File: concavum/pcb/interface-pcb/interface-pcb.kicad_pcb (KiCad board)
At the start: 2 copper layers, 36 x 42 mm, 11 parts, among them J1 Audio_Jack, J2 FPC_connector, U1 Adafruit_KB2040, U2 MCP23017/MCP23018

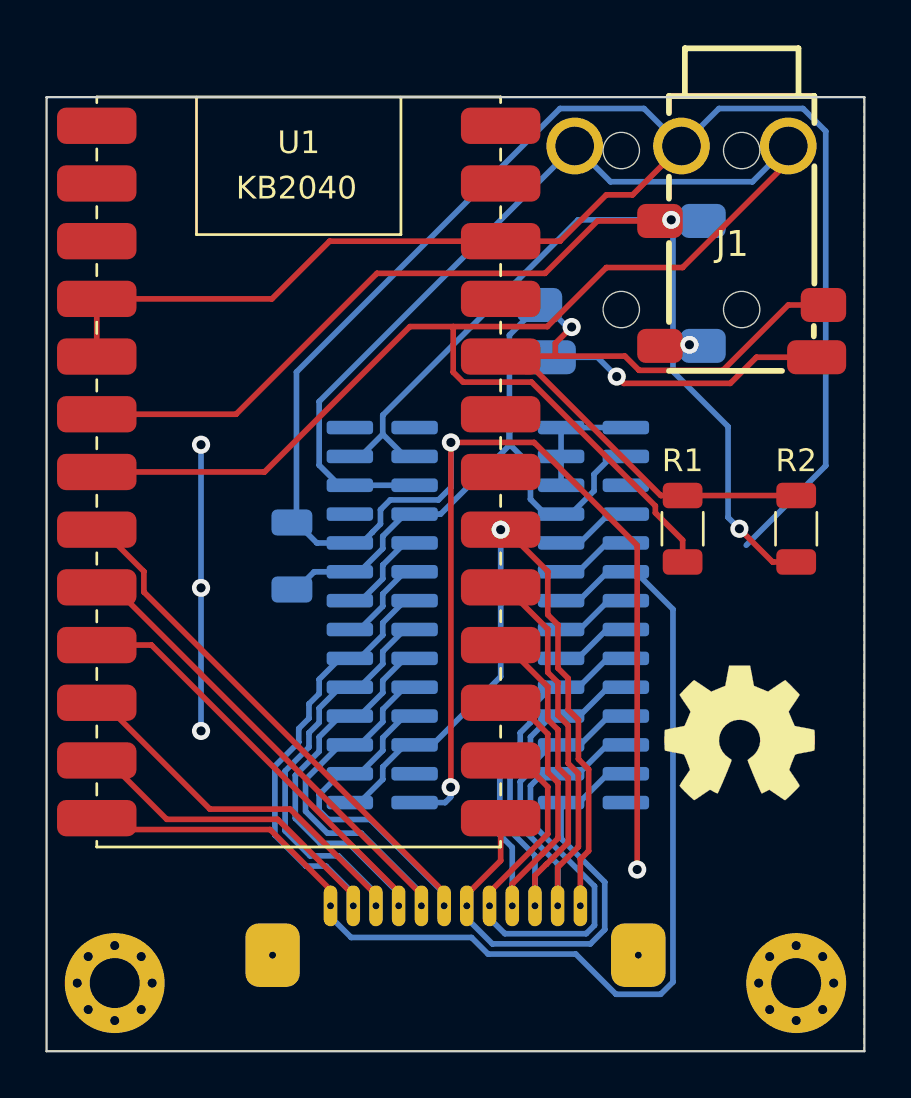
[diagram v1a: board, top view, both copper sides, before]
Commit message: Use the PCA9555 port expander for the right half
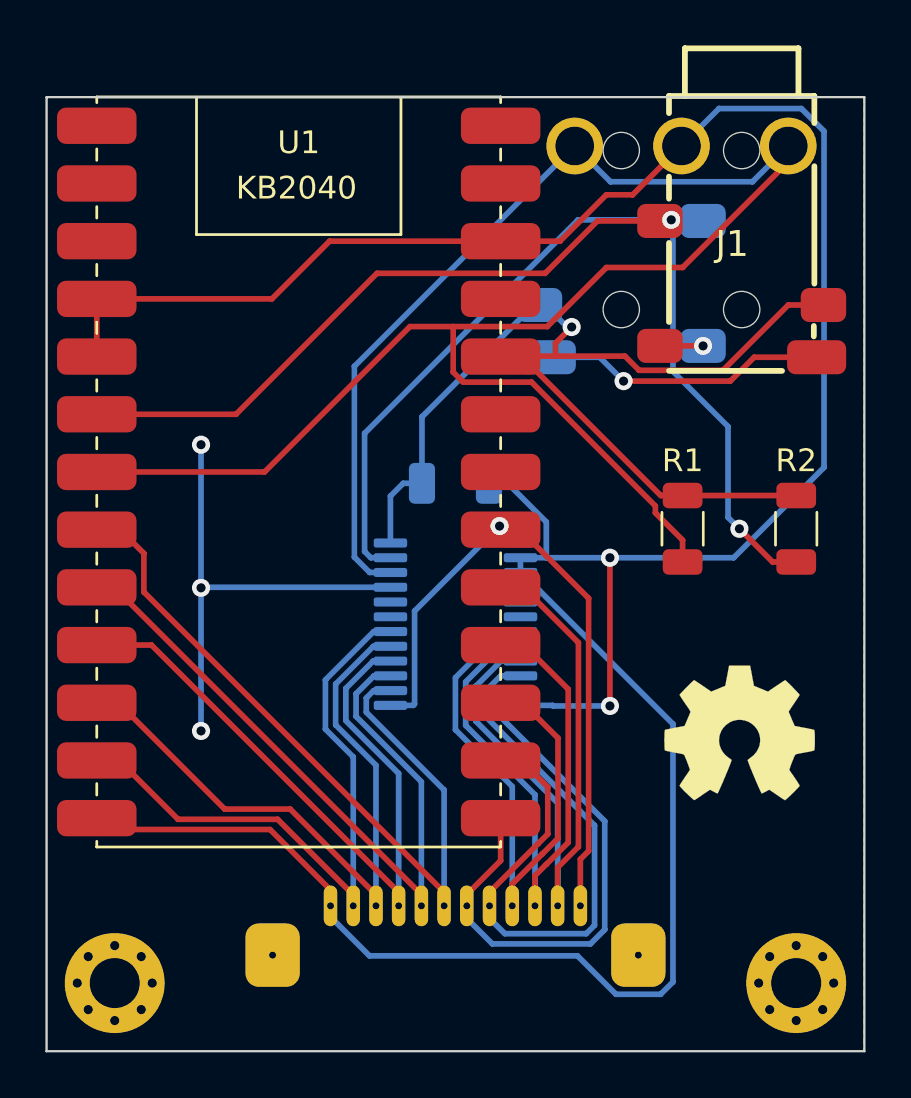
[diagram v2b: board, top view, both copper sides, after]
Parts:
- C1: value 100n -> 10u
- U2: value MCP23017/MCP23018 -> PCA9555PW; footprint Custom:MCP23017_SO_MCP23018_SO -> Package_SO:TSSOP-24_4.4x7.8mm_P0.65mm
- moved C1 7.88 mm to (151.0, 93.0), turned to 0 degrees
- moved REF** 0.73 mm to (139.7, 83.5)
- moved U2 0.40 mm to (151.0, 99.2), turned to 180 degrees
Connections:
- U2 pad 1: /COL6 -> unconnected-(U2-~{INT}-Pad1)
- U2 pad 10: GND -> /ROW3
- U2 pad 11: unconnected-(U2-Pad11) -> /ROW2
- U2 pad 12: /SCL -> GND
- U2 pad 13: /SDA -> /COL6
- U2 pad 14: unconnected-(U2-Pad14) -> /COL5
- U2 pad 15: GND -> /COL4
- U2 pad 16: unconnected-(U2-Pad16) -> /COL3
- U2 pad 17: unconnected-(U2-Pad17) -> /COL2
- U2 pad 18: +3V3 -> /COL1
- U2 pad 2: /COL5 -> GND
- U2 pad 21: /ROW1 -> GND
- U2 pad 22: unconnected-(U2-Pad22) -> /SCL
- U2 pad 23: unconnected-(U2-Pad23) -> /SDA
- U2 pad 24: /ROW4 -> +3V3
- U2 pad 3: /COL4 -> GND
- U2 pad 4: /COL3 -> /ROW1
- U2 pad 5: /COL2 -> unconnected-(U2-IO0_1-Pad5)
- U2 pad 6: /COL1 -> unconnected-(U2-IO0_2-Pad6)
- U2 pad 7: unconnected-(U2-Pad7) -> /ROW4
- U2 pad 8: unconnected-(U2-Pad8) -> /ROW5
- U2 pad 9: +3V3 -> /ROW6
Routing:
- net GND: track 158.2 -> 105.1 mm, vias 6 -> 5
- net +3V3: track 64.1 -> 48.4 mm
- net /COL6: track 34.2 -> 29.3 mm
- net /COL1: track 32.9 -> 28.4 mm
- net unconnected-(U2-Pad8): track 4.25 -> 0.00 mm
- net unconnected-(U2-Pad7): track 4.22 -> 0.00 mm
- net /COL2: track 33.9 -> 29.9 mm
- net /ROW2: track 21.6 -> 25.3 mm
- net /COL3: track 34.8 -> 31.4 mm
- net unconnected-(U2-Pad23): track 3.38 -> 0.00 mm
- net unconnected-(U2-Pad22): track 3.38 -> 0.00 mm
- net unconnected-(U2-IO1_7-Pad20): track 3.38 -> 0.00 mm
- net unconnected-(U2-IO1_6-Pad19): track 3.38 -> 0.00 mm
- net /COL4: track 35.7 -> 32.8 mm
- net /SDA: track 69.1 -> 71.5 mm
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
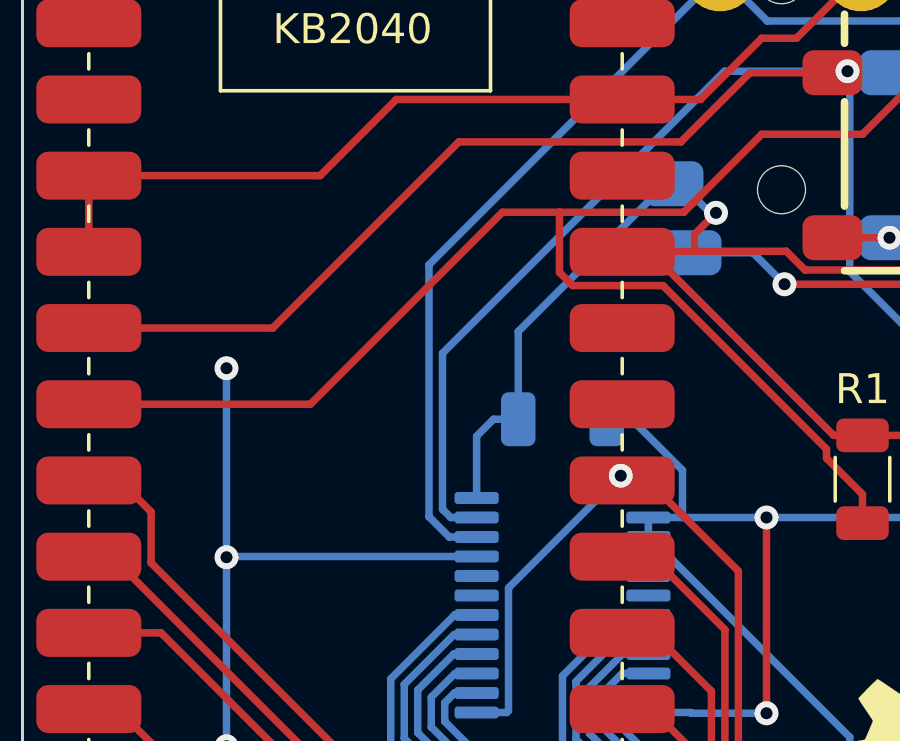
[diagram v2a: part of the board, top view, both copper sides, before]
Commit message: Change capacitor footprint to 0603
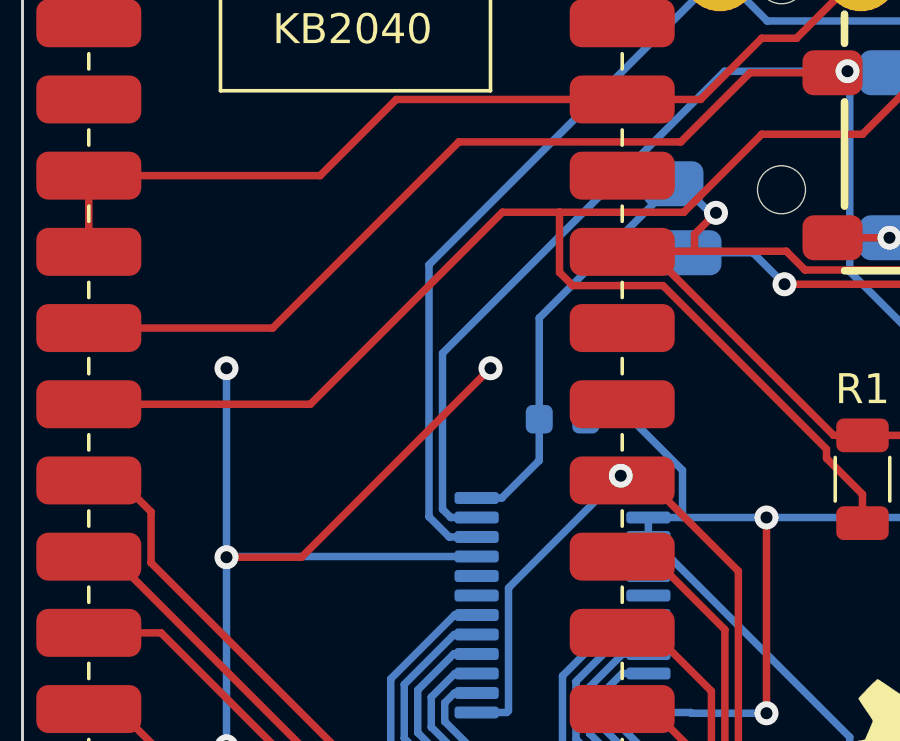
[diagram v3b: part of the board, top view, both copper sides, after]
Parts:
- C1: footprint Capacitor_SMD:C_1206_3216Metric -> Capacitor_SMD:C_0603_1608Metric
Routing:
- net GND: track 105.1 -> 116.5 mm, vias 5 -> 6
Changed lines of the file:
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@@
 		(sheetname "Root")
 		(sheetfile "interface-pcb.kicad_sch")
-		(attr exclude_from_pos_files)
+		(attr exclude_from_pos_files exclude_from_bom)
 		(fp_circle
 			(center 0 0)
@@
 		(sheetname "Root")
 		(sheetfile "interface-pcb.kicad_sch")
-		(attr through_hole)
+		(attr through_hole exclude_from_pos_files exclude_from_bom)
 		(fp_line
 			(start -6.85 8.5)
@@
 		(sheetname "Root")
 		(sheetfile "interface-pcb.kicad_sch")
-		(attr through_hole)
+		(attr through_hole exclude_from_pos_files exclude_from_bom)
 		(fp_line
 			(start -9.8 -1.2)
@@
 		(sheetname "Root")
 		(sheetfile "interface-pcb.kicad_sch")
-		(attr exclude_from_pos_files)
+		(attr exclude_from_pos_files exclude_from_bom)
 		(fp_circle
 			(center 0 0)
@@
 		(sheetname "Root")
 		(sheetfile "interface-pcb.kicad_sch")
-		(attr smd)
+		(attr smd exclude_from_pos_files exclude_from_bom)
 		(fp_line
 			(start -8.89 -16.51)
@@
 		(sheetname "Root")
 		(sheetfile "interface-pcb.kicad_sch")
-		(attr smd)
+		(attr smd exclude_from_pos_files exclude_from_bom)
 		(fp_line
 			(start -0.727064 -0.91)
@@
 		(sheetname "Root")
 		(sheetfile "interface-pcb.kicad_sch")
-		(attr smd)
+		(attr smd exclude_from_pos_files exclude_from_bom)
 		(fp_line
 			(start -0.727064 -0.91)
@@
 		)
 	)
-	(footprint "Capacitor_SMD:C_1206_3216Metric"
+	(footprint "Capacitor_SMD:C_0603_1608Metric"
 		(layer "B.Cu")
 		(at 151 93)
-		(descr "Capacitor SMD 1206 (3216 Metric), square (rectangular) end terminal, IPC_7351 nominal, (Body size source: IPC-SM-782 page 76, https://www.pcb-3d.com/wordpress/wp-content/uploads/ipc-sm-782a_amendment_1_and_2.pdf), generated with kicad-footprint-generator")
+		(descr "Capacitor SMD 0603 (1608 Metric), square (rectangular) end terminal, IPC_7351 nominal, (Body size source: IPC-SM-782 page 76, https://www.pcb-3d.com/wordpress/wp-content/uploads/ipc-sm-782a_amendment_1_and_2.pdf), generated with kicad-footprint-generator")
 		(tags "capacitor")
 		(property "Reference" "C1"
-			(at 0.1 -2 0)
+			(at 0 1.43 180)
 			(layer "B.SilkS")
 			(effects
@@
 		)
 		(property "Value" "10u"
-			(at -3.1 0.1 -90)
+			(at 0 -1.43 180)
 			(layer "B.Fab")
 			(effects
@@
 			)
 		)
-		(property "Footprint" "Capacitor_SMD:C_1206_3216Metric"
-			(at 0 0 0)
-			(layer "F.Fab")
+		(property "Footprint" "Capacitor_SMD:C_0603_1608Metric"
+			(at 0 0 180)
+			(unlocked yes)
+			(layer "B.Fab")
 			(hide yes)
 			(effects
@@
 					(thickness 0.15)
 				)
+				(justify mirror)
 			)
 		)
 		(property "Datasheet" ""
-			(at 0 0 0)
-			(layer "F.Fab")
+			(at 0 0 180)
+			(unlocked yes)
+			(layer "B.Fab")
 			(hide yes)
 			(effects
@@
 					(thickness 0.15)
 				)
+				(justify mirror)
 			)
 		)
 		(property "Description" ""
-			(at 0 0 0)
-			(layer "F.Fab")
+			(at 0 0 180)
+			(unlocked yes)
+			(layer "B.Fab")
 			(hide yes)
 			(effects
@@
 					(thickness 0.15)
 				)
+				(justify mirror)
 			)
 		)
@@
 		(attr smd)
 		(fp_line
-			(start -0.711252 -0.91)
-			(end 0.711252 -0.91)
+			(start 0.14058 -0.51)
+			(end -0.14058 -0.51)
 			(stroke
 				(width 0.12)
@@
 		)
 		(fp_line
-			(start -0.711252 0.91)
-			(end 0.711252 0.91)
+			(start 0.14058 0.51)
+			(end -0.14058 0.51)
 			(stroke
 				(width 0.12)
@@
 		)
 		(fp_line
-			(start -2.3 -1.15)
-			(end -2.3 1.15)
+			(start -1.48 -0.73)
+			(end 1.48 -0.73)
 			(stroke
 				(width 0.05)
@@
 		)
 		(fp_line
-			(start -2.3 1.15)
-			(end 2.3 1.15)
+			(start -1.48 0.73)
+			(end -1.48 -0.73)
 			(stroke
 				(width 0.05)
@@
 		)
 		(fp_line
-			(start 2.3 -1.15)
-			(end -2.3 -1.15)
+			(start 1.48 -0.73)
+			(end 1.48 0.73)
 			(stroke
 				(width 0.05)
@@
 		)
 		(fp_line
-			(start 2.3 1.15)
-			(end 2.3 -1.15)
+			(start 1.48 0.73)
+			(end -1.48 0.73)
 			(stroke
 				(width 0.05)
@@
 		)
 		(fp_line
-			(start -1.6 -0.8)
-			(end -1.6 0.8)
+			(start -0.8 -0.4)
+			(end 0.8 -0.4)
 			(stroke
 				(width 0.1)
@@
 		)
 		(fp_line
-			(start -1.6 0.8)
-			(end 1.6 0.8)
+			(start -0.8 0.4)
+			(end -0.8 -0.4)
 			(stroke
 				(width 0.1)
@@
 		)
 		(fp_line
-			(start 1.6 -0.8)
-			(end -1.6 -0.8)
+			(start 0.8 -0.4)
+			(end 0.8 0.4)
 			(stroke
 				(width 0.1)
@@
 		)
 		(fp_line
-			(start 1.6 0.8)
-			(end 1.6 -0.8)
+			(start 0.8 0.4)
+			(end -0.8 0.4)
 			(stroke
 				(width 0.1)
@@
 		)
 		(fp_text user "${REFERENCE}"
-			(at 0 0 0)
+			(at 0 0 180)
 			(layer "B.Fab")
 			(effects
 				(font
-					(size 0.8 0.8)
-					(thickness 0.12)
+					(size 0.4 0.4)
+					(thickness 0.06)
 				)
 				(justify mirror)
@@
 		)
 		(pad "1" smd roundrect
-			(at -1.475 0)
-			(size 1.15 1.8)
+			(at -0.775 0)
+			(size 0.9 0.95)
 			(layers "B.Cu" "B.Paste" "B.Mask")
-			(roundrect_rratio 0.217391)
+			(roundrect_rratio 0.25)
 			(net 3 "+3V3")
 			(pintype "passive")
 		)
 		(pad "2" smd roundrect
-			(at 1.475 0)
-			(size 1.15 1.8)
+			(at 0.775 0)
+			(size 0.9 0.95)
 			(layers "B.Cu" "B.Paste" "B.Mask")
-			(roundrect_rratio 0.217391)
+			(roundrect_rratio 0.25)
 			(net 1 "GND")
 			(pintype "passive")
 		)
-		(model "${KICAD6_3DMODEL_DIR}/Capacitor_SMD.3dshapes/C_1206_3216Metric.wrl"
+		(model "${KICAD8_3DMODEL_DIR}/Capacitor_SMD.3dshapes/C_0603_1608Metric.wrl"
 			(offset
 				(xyz 0 0 0)
@@
 	)
 	(segment
+		(start 142.3 97.6)
+		(end 148.6 91.3)
+		(width 0.25)
+		(layer "F.Cu")
+		(net 1)
+	)
+	(segment
 		(start 135.21 84.88)
 		(end 142.92 84.88)
@@
 	)
 	(segment
+		(start 139.8 97.6)
+		(end 142.3 97.6)
+		(width 0.25)
+		(layer "F.Cu")
+		(net 1)
+	)
+	(segment
 		(start 135.21 87.42)
 		(end 135.21 84.88)
@@
 	)
 	(via
+		(at 148.6 91.3)
+		(size 0.8)
+		(drill 0.4)
+		(layers "F.Cu" "B.Cu")
+		(net 1)
+	)
+	(via
 		(at 157.8 102.8)
 		(size 0.8)
@@
 	)
 	(segment
-		(start 154.45 85.15)
-		(end 154.7 85.15)
-		(width 0.25)
-		(layer "B.Cu")
-		(net 3)
-	)
-	(segment
 		(start 155.919424 86.119424)
 		(end 156.116115 86.119424)
@@
 	)
 	(segment
-		(start 149.525 93)
-		(end 149.525 90.075)
+		(start 150.225 93)
+		(end 150.225 94.375)
 		(width 0.25)
 		(layer "B.Cu")
@@
 	)
 	(segment
-		(start 148.1375 95.625)
-		(end 148.1375 93.5625)
+		(start 150.225 89.625)
+		(end 150.225 93)
 		(width 0.25)
 		(layer "B.Cu")
@@
 	)
 	(segment
-		(start 148.1375 93.5625)
-		(end 148.7 93)
+		(start 150.225 94.375)
+		(end 148.975 95.625)
 		(width 0.25)
 		(layer "B.Cu")
@@
 	)
 	(segment
-		(start 148.7 93)
-		(end 149.525 93)
+		(start 154.7 85.15)
+		(end 150.225 89.625)
 		(width 0.25)
 		(layer "B.Cu")
@@
 	)
 	(segment
-		(start 149.525 90.075)
-		(end 154.45 85.15)
+		(start 148.975 95.625)
+		(end 148.1375 95.625)
 		(width 0.25)
 		(layer "B.Cu")

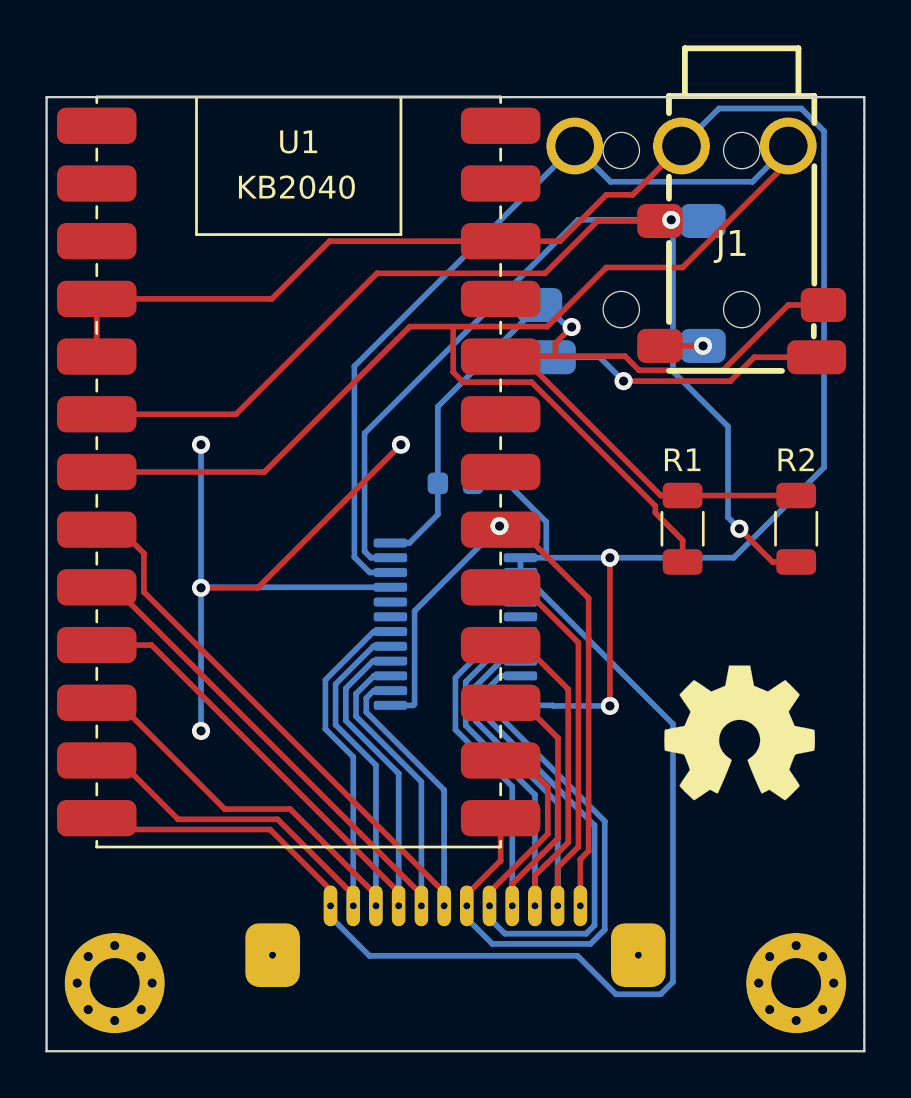
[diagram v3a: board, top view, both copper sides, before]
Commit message: Move capacitor closer to IC and add second QR code
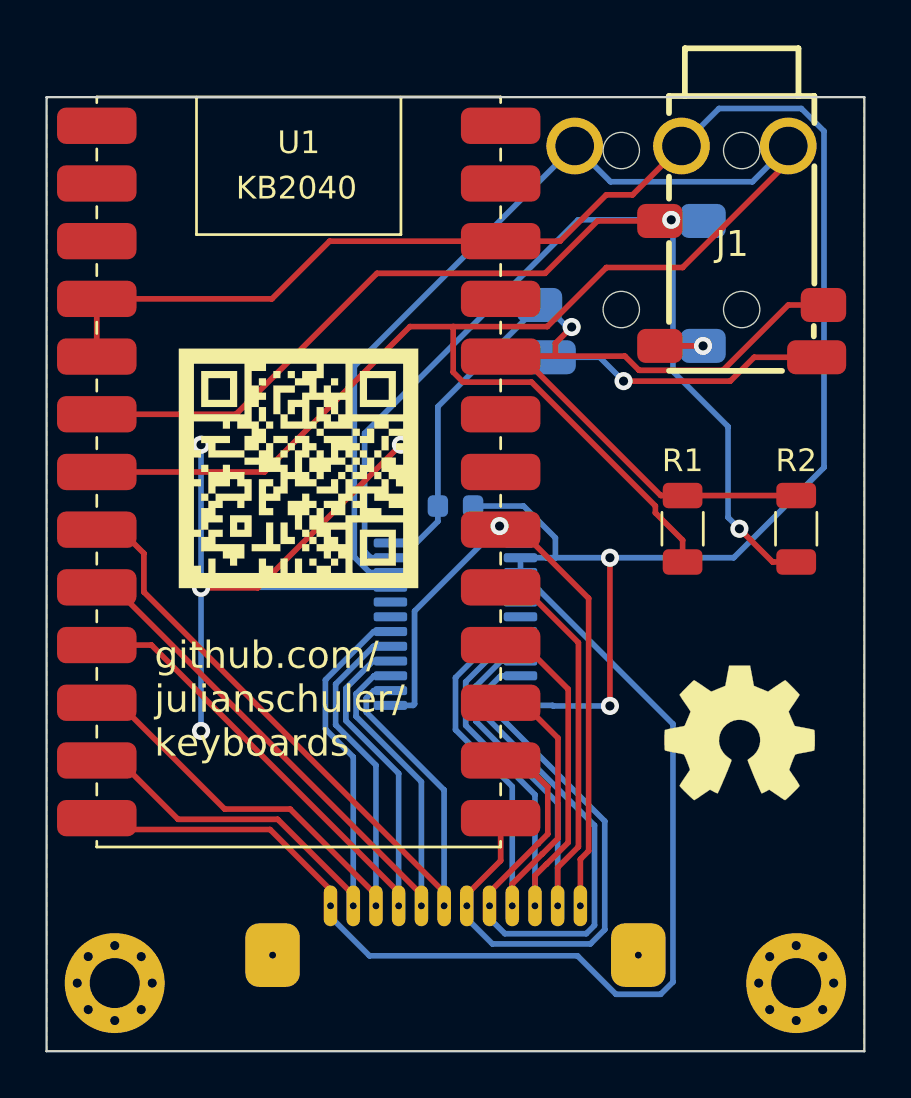
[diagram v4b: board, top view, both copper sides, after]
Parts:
- moved C1 1.00 mm to (151.0, 94.0)
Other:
- board text added: "github.com/ julianschuler/ keyboards"
